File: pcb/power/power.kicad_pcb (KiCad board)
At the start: 2 copper layers, 50 x 40 mm, 176 parts, among them CON1 BARREL_JACK, P1 CONN_01X04, P2 CONN_01X04, P3 CONN_01X04, P4 USB_A, P5 CONN_01X03, P6 CONN_01X03, Q1 MMBT3904, Q2 MMBT3904, Q3 MMBT3904, Q4 MMBT3904, Q5 MMBT3904, Q6 MMBT3904, Q7 DMG2305UX, Q8 DMG2305UX, Q9 DMG2305UX, U1 LM2840, U2 TS30012, U3 LM324QT

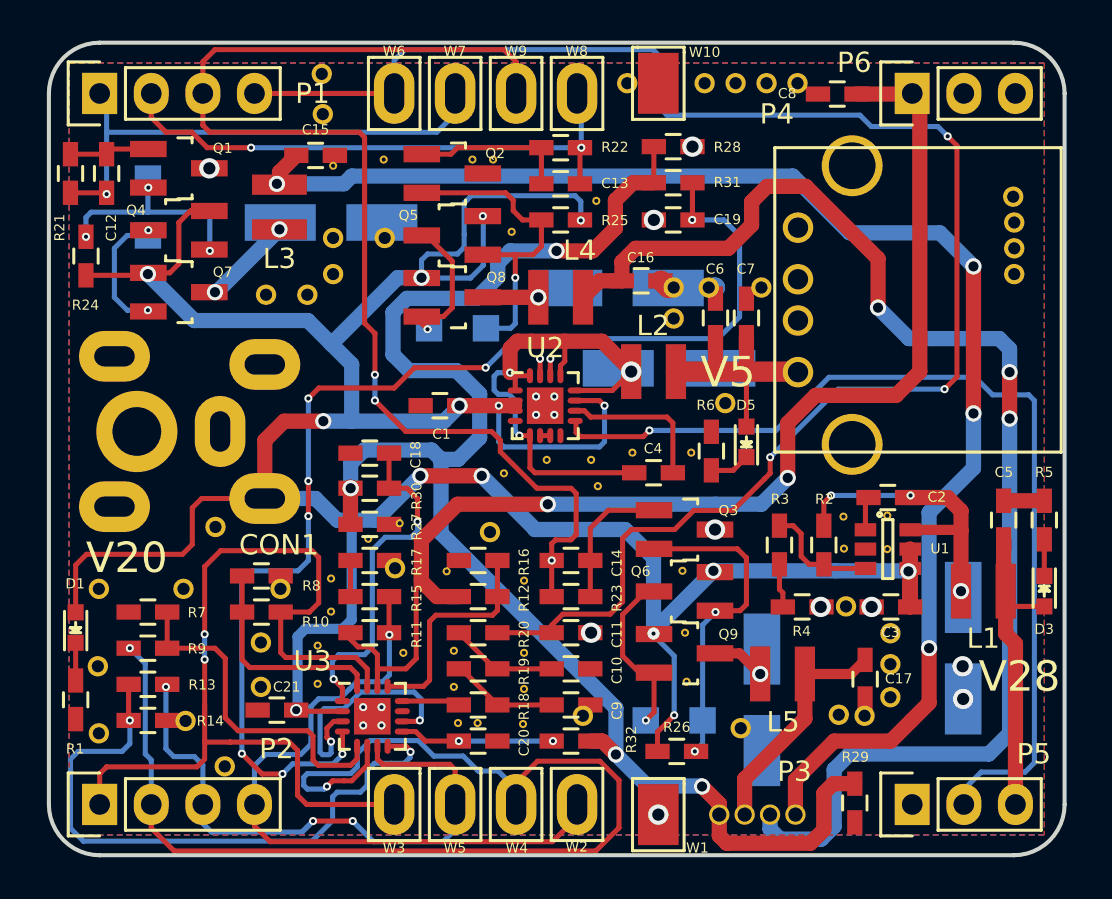
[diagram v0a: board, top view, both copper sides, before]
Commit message: Only thing missing now in the 3D model is one diode type.
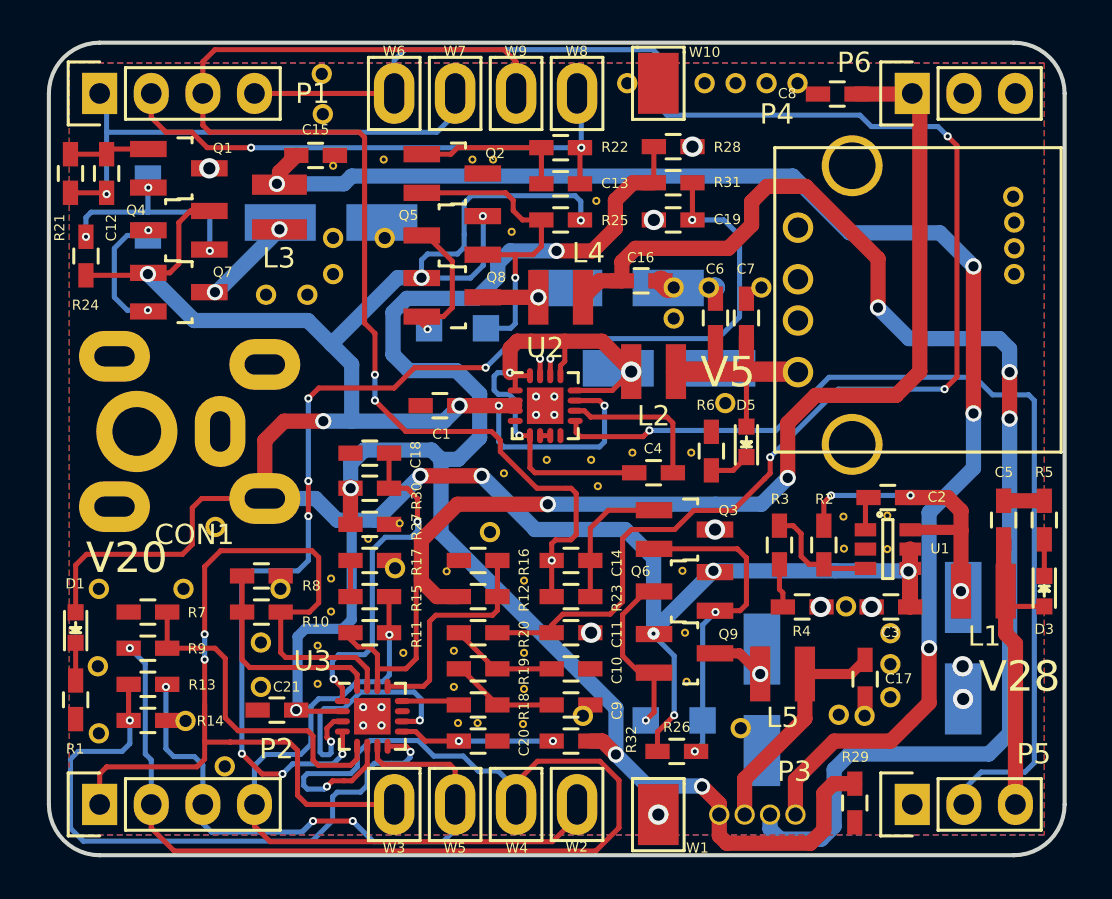
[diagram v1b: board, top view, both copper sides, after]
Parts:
- removed the G*** at (152.1, 112.0)
- turned G*** to 0 degrees
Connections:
- U2 pad 17: GND -> (no net)
- U3 pad 17: GND -> (no net)
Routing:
- net GND: track 6.92 -> 6.54 mm, vias 20 -> 12
- net (no net): track 0.00 -> 0.38 mm, vias 0 -> 8

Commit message: Started completely over with the layout, as the OLED would not fit anymore. Also introduced a USB DCP Controller and found a stupid bug in the LED driver.
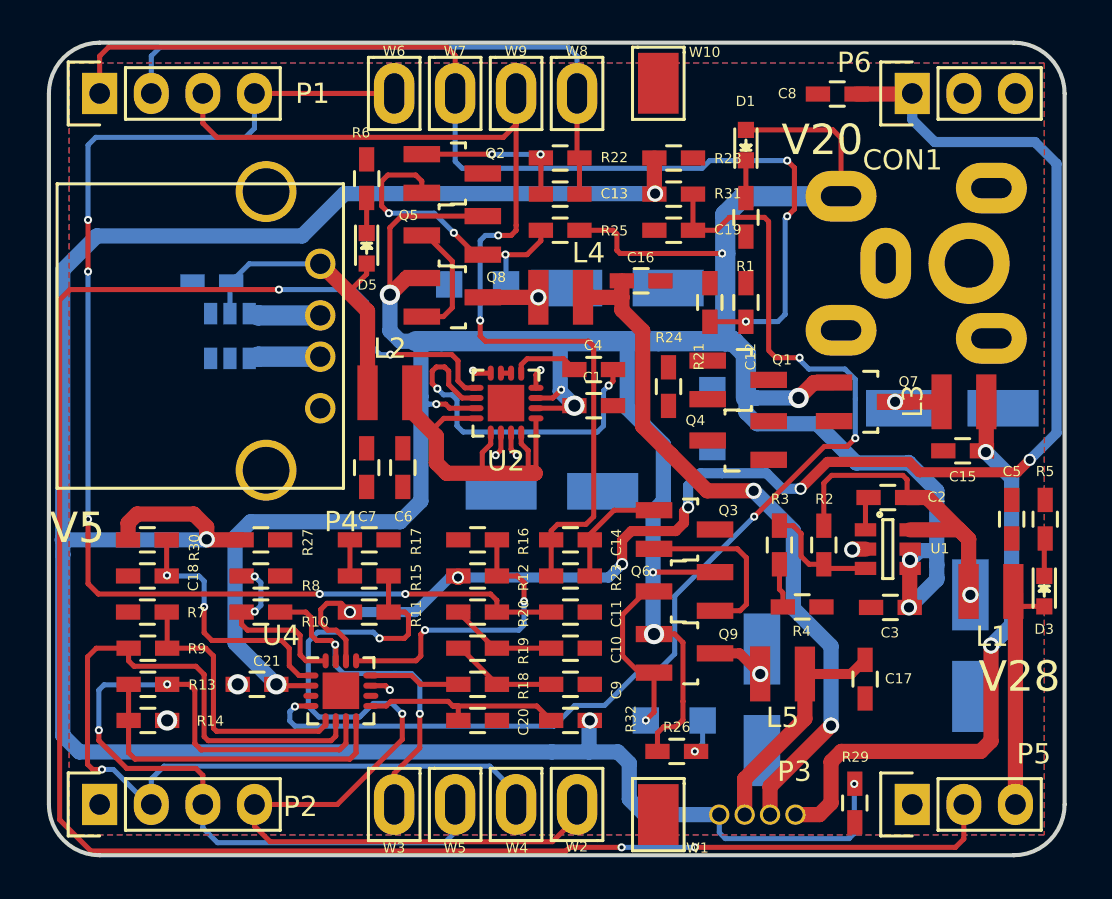
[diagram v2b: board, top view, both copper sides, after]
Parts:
- removed G***: LOGO, Additional:UU
- removed REF** (x35): Via_GND_04, Additional:Via_GND_04
- removed REF**: Via_GND_1, Additional:Via_GND_1
- removed REF** (x40): Vian_GND_1, Additional:Via_GND_1
- added C22: C, Capacitors_SMD:C_0603_HandSoldering, B.Cu at (138.0, 96.8)
- added U3: TPS2514ADBV, TO_SOT_Packages_SMD:SOT-23-6, B.Cu at (138.9, 99.4)
- moved D1 40.7 mm to (164.3, 90.0)
- moved R1 40.7 mm to (164.3, 93.6)
- moved L3 35.0 mm to (175.0, 102.7), turned to 90 degrees
- moved C15 35.0 mm to (175.0, 105.1), turned to 180 degrees
- moved Q7 34.2 mm to (170.2, 102.7)
- moved CON1 33.8 mm to (171.2, 95.9), turned to 180 degrees
- moved R21 32.1 mm to (162.5, 97.8)
- moved C12 32.1 mm to (164.3, 97.8)
- moved D9 31.9 mm to (174.5, 103.0)
- moved D6 29.7 mm to (162.7, 103.5)
- moved Q1 29.4 mm to (163.9, 101.6)
- moved Q4 29.4 mm to (163.9, 104.6)
- moved R24 29.4 mm to (160.5, 101.9), turned to 90 degrees
- moved P4 24.1 mm to (143.4, 95.9), turned to 270 degrees
- moved R6 21.6 mm to (145.6, 91.7)
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- renumbered U3 to U4
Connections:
- P4 pad 2: Net-(P4-Pad2) -> /Bucket Converters/DM1
- P4 pad 3: Net-(P4-Pad3) -> /Bucket Converters/DP1
- U2 pad 7: Net-(U2-Pad6) -> Net-(U2-Pad7)
- U4 pad 10: Net-(U3-Pad10) -> Net-(U4-Pad10)
- U4 pad 3: Net-(U3-Pad10) -> Net-(U4-Pad3)
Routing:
- net 5V_EN: track 47.7 -> 97.1 mm, vias 1 -> 4
- net LED_GND: track 74.5 -> 116.9 mm
- net LED_R: track 70.5 -> 30.2 mm, vias 4 -> 2
- net ADC_R: track 46.8 -> 17.0 mm
- net LED_B: track 64.6 -> 35.0 mm, vias 3 -> 2
- net PWM_R: track 27.1 -> 53.3 mm, vias 1 -> 3
- net PWM_OLED: track 81.6 -> 62.4 mm, vias 3 -> 5
- net ADC_B: track 62.3 -> 47.3 mm, vias 2 -> 1
- net Net-(R13-Pad1): track 31.0 -> 16.4 mm, vias 2 -> 0
- net Net-(U3-Pad10): track 12.3 -> 0.00 mm, vias 2 -> 0
- net ADC_OLED: track 33.8 -> 45.9 mm, vias 1 -> 2
- net ADC_G: track 30.1 -> 41.6 mm, vias 3 -> 2
- net Net-(D6-Pad1): track 11.1 -> 0.00 mm, vias 3 -> 0
- net VOLED: track 61.3 -> 71.7 mm, vias 2 -> 6
- net PWM_G: track 61.6 -> 51.2 mm, vias 3 -> 2
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
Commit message: Fixed the bug. Now workin with differential amplifiers. Started over once more with the layout.
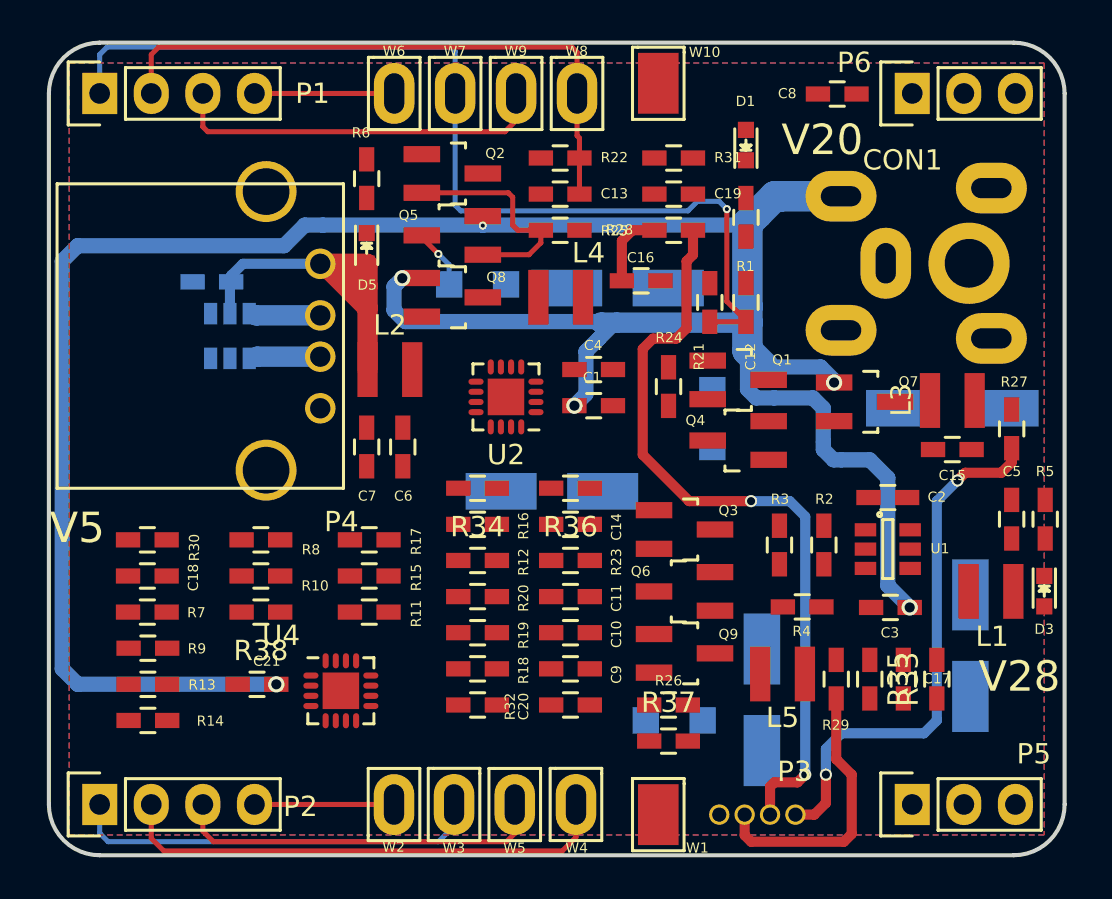
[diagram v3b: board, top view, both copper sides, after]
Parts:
- added R33: 3.9k, Additional:R_0603_HandSoldering_Same_As_C, F.Cu at (170.4, 116.3)
- added R34: 3.9k, Additional:R_0603_HandSoldering_Same_As_C, F.Cu at (151.1, 106.9)
- added R35: 120k, Additional:R_0603_HandSoldering_Same_As_C, F.Cu at (173.7, 116.3)
- added R36: 120k, Additional:R_0603_HandSoldering_Same_As_C, F.Cu at (155.7, 106.9)
- added R37: 120k, Additional:R_0603_HandSoldering_Same_As_C, F.Cu at (160.5, 119.4)
- added R38: 3.9k, Additional:R_0603_HandSoldering_Same_As_C, F.Cu at (140.4, 113.0)
- C22: value C -> 0.1u
- moved R27 37.4 mm to (177.4, 104.0), turned to 90 degrees
- moved W2 9.01 mm to (147.0, 122.5)
- moved R29 6.16 mm to (168.8, 116.3), turned to 90 degrees
- moved R28 3.56 mm to (160.8, 94.2), turned to 180 degrees
- moved W3 2.95 mm to (149.9, 122.5)
- moved W4 2.95 mm to (155.9, 122.5)
- moved W5 2.93 mm to (152.9, 122.5)
- moved R26 2.32 mm to (160.5, 117.6)
- moved C17 1.88 mm to (172.1, 116.3)
- moved R10 1.78 mm to (140.4, 111.3)
- moved R31 1.78 mm to (160.8, 90.7)
- moved C19 1.78 mm to (160.8, 92.5)
- moved R8 1.78 mm to (140.4, 109.5)
- moved L2 1.14 mm to (146.8, 101.1)
- moved C6 1.02 mm to (147.4, 104.9)
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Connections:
- net /Bucket Converters/DM1 renamed D-
- net /Bucket Converters/DP1 renamed D+
- C1 pad 2: GND -> LED_GND
- C10 pad 2: GND -> LED_GND
- C11 pad 2: GND -> LED_GND
- C15 pad 1: LED_R -> Net-(C15-Pad1)
- C15 pad 2: GND -> LED_GND
- C16 pad 1: LED_B -> Net-(C16-Pad1)
- C16 pad 2: GND -> LED_GND
- C17 pad 1: LED_G -> Net-(C17-Pad1)
- C17 pad 2: GND -> LED_GND
- C18 pad 1: GND -> OPAMP_R_P
- C18 pad 2: /LEDs/LED Driver 3 Chan. /OPAMP_R -> LED_R
- C19 pad 1: GND -> OPAMP_B_P
- C19 pad 2: /LEDs/LED Driver 3 Chan. /OPAMP_B -> LED_B
- C20 pad 1: GND -> OPAMP_G_P
- C20 pad 2: /LEDs/LED Driver 3 Chan. /OPAMP_G -> LED_G
- C21 pad 1: GND -> LED_GND
- C22 pad 2: GND -> LED_GND
- C3 pad 2: GND -> LED_GND
- C5 pad 2: GND -> LED_GND
- C6 pad 2: GND -> LED_GND
- C7 pad 2: GND -> LED_GND
- C8 pad 1: GND -> LED_GND
- C9 pad 2: GND -> LED_GND
- CON1 pad 2: GND -> LED_GND
- CON1 pad 3: GND -> LED_GND
- D10 pad 2: GND -> LED_GND
- D11 pad 2: GND -> LED_GND
- D2 pad 2: GND -> LED_GND
- D4 pad 2: GND -> LED_GND
- D9 pad 2: GND -> LED_GND
- L3 pad 2: LED_R -> Net-(C15-Pad1)
- L4 pad 2: LED_B -> Net-(C16-Pad1)
- L5 pad 2: LED_G -> Net-(C17-Pad1)
- P4 pad 4: GND -> LED_GND
- P4 pad 5: GND -> LED_GND
- P5 pad 1: GND -> LED_GND
- P6 pad 2: GND -> LED_GND
- P6 pad 3: GND -> LED_GND
- Q1 pad 3: GND -> LED_GND
- Q2 pad 3: GND -> LED_GND
- Q3 pad 3: GND -> LED_GND
- R1 pad 2: GND -> LED_GND
- R14 pad 1: GND -> OPAMP_G_P
- R16 pad 1: GND -> LED_GND
- R17 pad 1: GND -> LED_GND
- R27 pad 1: LED_GND -> LED_R
- R27 pad 2: GND -> Net-(C15-Pad1)
- R28 pad 1: LED_GND -> LED_B
- R28 pad 2: GND -> Net-(C16-Pad1)
- R29 pad 1: LED_GND -> LED_G
- R29 pad 2: GND -> Net-(C17-Pad1)
- R30 pad 1: /LEDs/LED Driver 3 Chan. /OPAMP_R -> Net-(C15-Pad1)
- R30 pad 2: LED_GND -> OPAMP_R_P
- R31 pad 1: /LEDs/LED Driver 3 Chan. /OPAMP_B -> Net-(C16-Pad1)
- R31 pad 2: LED_GND -> OPAMP_B_P
- R32 pad 1: /LEDs/LED Driver 3 Chan. /OPAMP_G -> Net-(C17-Pad1)
- R32 pad 2: LED_GND -> OPAMP_G_P
- R4 pad 2: GND -> LED_GND
- R5 pad 2: GND -> LED_GND
- R6 pad 2: GND -> LED_GND
- R7 pad 2: GND -> OPAMP_B_P
- R8 pad 2: GND -> OPAMP_R_P
- U1 pad 2: GND -> LED_GND
- U2 pad 14: GND -> LED_GND
- U2 pad 15: GND -> LED_GND
- U2 pad 4: GND -> LED_GND
- U2 pad 8: GND -> Net-(U2-Pad8)
- U3 pad 2: GND -> LED_GND
- U4 pad 1: /LEDs/LED Driver 3 Chan. /OPAMP_R -> Net-(R33-Pad1)
- U4 pad 11: GND -> LED_GND
- U4 pad 4: /LEDs/LED Driver 3 Chan. /OPAMP_B -> Net-(R34-Pad1)
- U4 pad 9: /LEDs/LED Driver 3 Chan. /OPAMP_G -> Net-(R37-Pad1)
- W1 pad 1: GND -> LED_GND
- W10 pad 1: GND -> LED_GND
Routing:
- net LED_GND: track 116.9 -> 0.00 mm, vias 4 -> 0
- net 5V_EN: track 97.1 -> 0.00 mm, vias 4 -> 0
- net VOLED: track 71.7 -> 0.00 mm, vias 6 -> 0
- net /LEDs/LED Driver 3 Chan. /OPAMP_B: track 57.0 -> 0.00 mm, vias 4 -> 0
- net PWM_OLED: track 62.4 -> 6.88 mm, vias 5 -> 0
- net ADC_OLED: track 45.9 -> 6.87 mm, vias 2 -> 0
- net PWM_G: track 51.2 -> 18.7 mm, vias 2 -> 0
- net V20: track 153.2 -> 128.4 mm, vias 11 -> 6
- net Net-(C4-Pad2): track 23.8 -> 0.00 mm
- net ADC_G: track 41.6 -> 18.5 mm, vias 2 -> 0
- net ADC_B: track 47.3 -> 24.7 mm, vias 1 -> 0
- net Net-(C4-Pad1): track 17.1 -> 0.00 mm, vias 2 -> 0
- net Net-(C2-Pad1): track 17.1 -> 0.00 mm, vias 1 -> 0
- net Net-(R13-Pad1): track 16.4 -> 0.00 mm
- net Net-(R12-Pad1): track 15.0 -> 0.00 mm, vias 2 -> 0
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
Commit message: Finished the layout almost (third time). Some via stitching still has to be done. Taking a look at heat disipation, too.
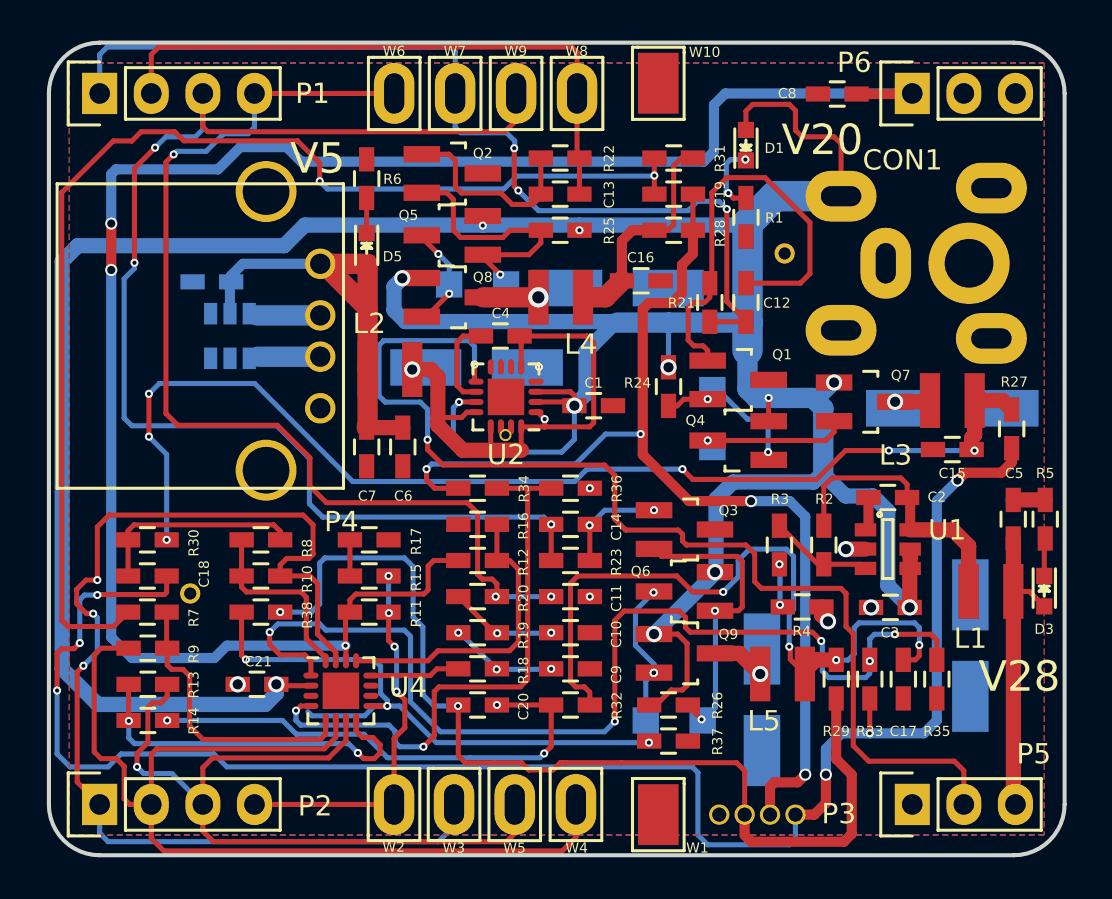
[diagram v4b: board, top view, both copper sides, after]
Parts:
- added REF**: Via_GND_04, Additional:Via_GND_06, F.Cu at (152.5, 104.3)
- added REF**: Via_GND_1, Additional:Via_GND_1, F.Cu at (166.2, 95.4)
- added REF**: Via_GND_1, Additional:Via_GND_1, F.Cu at (137.0, 112.1)
- moved D4 7.14 mm to (151.1, 101.0)
- moved C4 4.88 mm to (152.2, 99.4), turned to 0 degrees
- moved C5 0.08 mm to (177.5, 108.5)
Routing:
- net VOLED: track 0.00 -> 90.7 mm, vias 0 -> 3
- net OPAMP_B_P: track 0.00 -> 58.9 mm, vias 0 -> 2
- net LED_R: track 26.4 -> 83.6 mm, vias 2 -> 6
- net Net-(C15-Pad1): track 0.00 -> 56.1 mm, vias 0 -> 6
- net 5V_EN: track 0.00 -> 54.9 mm, vias 0 -> 2
- net Net-(R33-Pad1): track 0.00 -> 51.7 mm, vias 0 -> 5
- net V20: track 128.4 -> 178.9 mm, vias 6 -> 12
- net PWM_OLED: track 6.88 -> 51.8 mm, vias 0 -> 3
- net PWM_G: track 18.7 -> 63.4 mm, vias 0 -> 3
- net LED_G: track 13.6 -> 50.6 mm, vias 0 -> 2
- net ADC_R: track 20.4 -> 57.4 mm, vias 0 -> 3
- net Net-(C17-Pad1): track 0.00 -> 35.7 mm, vias 0 -> 4
- net Net-(R37-Pad1): track 0.00 -> 30.0 mm, vias 0 -> 3
- net Net-(R34-Pad1): track 0.00 -> 28.3 mm, vias 0 -> 2
- net Net-(C4-Pad2): track 0.00 -> 28.2 mm, vias 0 -> 2
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- added copper zone on B.Cu, net LED_GND
- added copper zone on F.Cu, net LED_GND
- removed copper zone on B.Cu, net GND
- removed copper zone on F.Cu, net GND
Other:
- board text added: "Swakeup Power Rev1"
- board text removed: "Swakeup Power Board v1.0"
